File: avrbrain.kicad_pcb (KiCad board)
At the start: 2 copper layers, 85 x 56 mm, 61 parts, among them J1 UPDI, J11 UEXT, J12 SM04B-SRSS-TB, J2 PORTD, J3 PORTG, J4 PORTE, J5 PORTA, J6 PORTB, J7 PORTC, J8 XKTF-0803-0, J9 U254-051T-4BH81-S2S, Q1 BSS138, SW1 RESET, SW3 PROG_EN, U1 AVR128DB64x-xPT, U2 AMS1117-3.3, U3 CH340C, U4 PCF8563T, Y1 32kHz

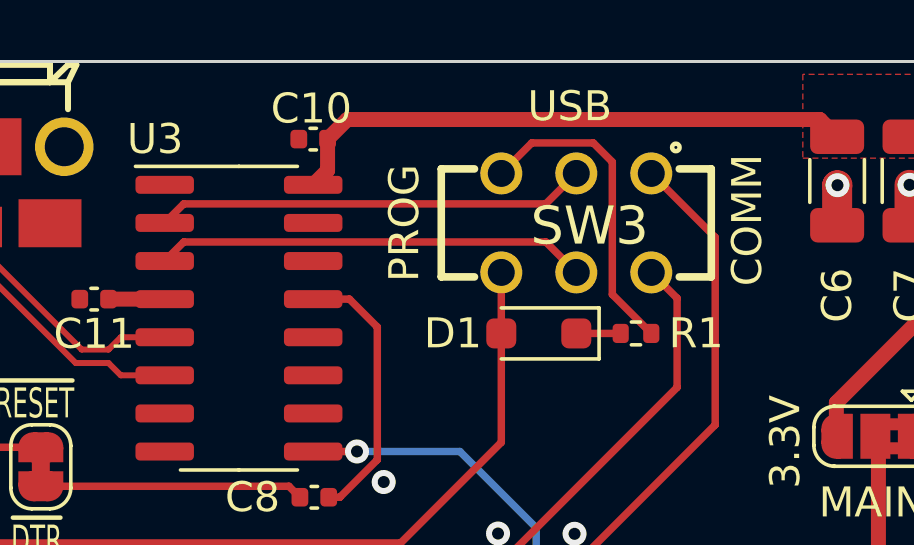
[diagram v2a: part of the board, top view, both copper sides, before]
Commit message: Put resistor before switch to avoid parasitic powering of the board
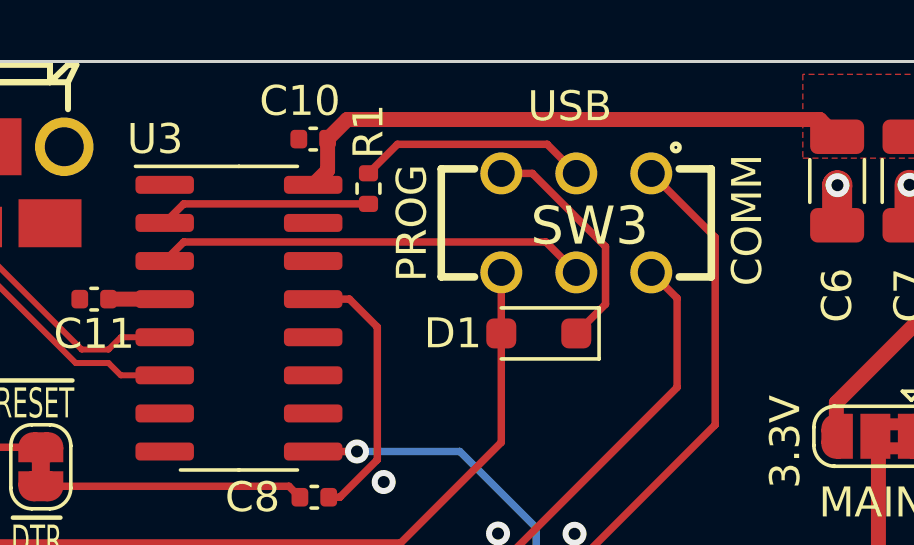
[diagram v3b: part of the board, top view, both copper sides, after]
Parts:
- R1: value 4.7K -> 1K
- moved R1 10.1 mm to (146.8, 85.2), turned to 90 degrees
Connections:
- R1 pad 1: Net-(SW3A-C) -> Net-(U3-TXD)
- R1 pad 2: Net-(D1-K) -> /Peripherals/USBTX
- SW3 pad 3: Net-(SW3A-C) -> Net-(D1-K)
- U3 pad 2: /Peripherals/USBTX -> Net-(U3-TXD)
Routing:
- net Net-(SW3A-C): track 10.6 -> 0.00 mm
- net Net-(U3-TXD): track 0.00 -> 7.06 mm
- net /Peripherals/USBTX: track 14.4 -> 7.73 mm
- net Net-(D1-K): track 1.48 -> 7.78 mm
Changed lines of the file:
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@@
   (net 79 "Net-(JP2-B)")
   (net 80 "Net-(JP3-B)")
-  (net 81 "Net-(SW3A-C)")
+  (net 81 "Net-(U3-TXD)")
   (net 82 "/Peripherals/USBTX")
   (net 83 "/Peripherals/USBRX")
@@
       (net 2 "GND") (pinfunction "GND") (pintype "power_in"))
     (pad "2" smd roundrect (at -2.475 -3.175) (size 1.95 0.6) (layers "F.Cu" "F.Paste" "F.Mask") (roundrect_rratio 0.25)
-      (net 82 "/Peripherals/USBTX") (pinfunction "TXD") (pintype "output"))
+      (net 81 "Net-(U3-TXD)") (pinfunction "TXD") (pintype "output"))
     (pad "3" smd roundrect (at -2.475 -1.905) (size 1.95 0.6) (layers "F.Cu" "F.Paste" "F.Mask") (roundrect_rratio 0.25)
       (net 83 "/Peripherals/USBRX") (pinfunction "RXD") (pintype "input"))
@@
       (net 82 "/Peripherals/USBTX") (pinfunction "B") (pintype "passive"))
     (pad "3" thru_hole circle (at 2.5 1.65 180) (size 1.4 1.4) (drill 0.9) (layers "*.Cu" "*.Mask")
-      (net 81 "Net-(SW3A-C)") (pinfunction "C") (pintype "passive"))
+      (net 49 "Net-(D1-K)") (pinfunction "C") (pintype "passive"))
     (pad "4" thru_hole circle (at -2.5 -1.65 180) (size 1.4 1.4) (drill 0.9) (layers "*.Cu" "*.Mask")
       (net 41 "TXF") (pinfunction "A") (pintype "passive"))
@@
     (fp_arc (start 4.02 5.42) (mid 4.121556 5.533647) (end 4.22 5.65)
       (stroke (width 0.05) (type solid)) (layer "F.CrtYd"))
-    (fp_arc (start 5.3 6.1) (mid 4.714387 5.984475) (end 4.22 5.65)
+    (fp_arc (start 5.3 6.1) (mid 4.714381 5.984481) (end 4.22 5.65)
       (stroke (width 0.05) (type solid)) (layer "F.CrtYd"))
     (fp_arc (start 7.25 -1.94) (mid 8.650198 0.005) (end 7.25 1.95)
       (stroke (width 0.05) (type solid)) (layer "F.CrtYd"))
-    (fp_arc (start 7.25 4.1) (mid 6.682004 5.496828) (end 5.3 6.1)
+    (fp_arc (start 7.25 4.1) (mid 6.682004 5.496829) (end 5.3 6.1)
       (stroke (width 0.05) (type solid)) (layer "F.CrtYd"))
     (fp_line (start -6.6 -3.4) (end -6.6 4.05)
@@
     (fp_arc (start 5.378013 5.447558) (mid 4.942442 5.378013) (end 4.6 5.1)
       (stroke (width 0.1) (type solid)) (layer "F.Fab"))
-    (fp_arc (start 6.6 4.1) (mid 6.222442 5.03735) (end 5.3 5.45)
+    (fp_arc (start 6.6 4.1) (mid 6.222443 5.037354) (end 5.3 5.45)
       (stroke (width 0.1) (type solid)) (layer "F.Fab"))
     (pad "1" thru_hole circle (at -6.6 0) (size 3 3) (drill 1.9) (layers "*.Cu" "*.Mask")
@@
   )
   (footprint "Resistor_SMD:R_0402_1005Metric" (layer "F.Cu")
-    (at 155.7285 90.043 180)
+    (at 146.812 85.215 90)
     (descr "Resistor SMD 0402 (1005 Metric), square (rectangular) end terminal, IPC_7351 nominal, (Body size source: IPC-SM-782 page 72, https://www.pcb-3d.com/wordpress/wp-content/uploads/ipc-sm-782a_amendment_1_and_2.pdf), generated with kicad-footprint-generator")
     (tags "resistor")
@@
     (property "ki_keywords" "R resistor")
     (attr smd)
-    (fp_text reference "R1" (at -2.0055 0) (layer "F.SilkS")
+    (fp_text reference "R1" (at 1.903 0 90) (layer "F.SilkS")
         (effects (font (size 1 1) (thickness 0.15)))
     )
-    (fp_text value "4.7K" (at 0 1.17) (layer "F.Fab")
+    (fp_text value "1K" (at 0 1.17 90) (layer "F.Fab")
         (effects (font (size 1 1) (thickness 0.15)))
     )
-    (fp_text user "${REFERENCE}" (at 0 0) (layer "F.Fab")
+    (fp_text user "${REFERENCE}" (at 0 0 90) (layer "F.Fab")
         (effects (font (size 0.26 0.26) (thickness 0.04)))
     )
@@
     (fp_line (start 0.525 0.27) (end -0.525 0.27)
       (stroke (width 0.1) (type solid)) (layer "F.Fab"))
-    (pad "1" smd roundrect (at -0.51 0 180) (size 0.54 0.64) (layers "F.Cu" "F.Paste" "F.Mask") (roundrect_rratio 0.25)
-      (net 81 "Net-(SW3A-C)") (pintype "passive"))
-    (pad "2" smd roundrect (at 0.51 0 180) (size 0.54 0.64) (layers "F.Cu" "F.Paste" "F.Mask") (roundrect_rratio 0.25)
-      (net 49 "Net-(D1-K)") (pintype "passive"))
+    (pad "1" smd roundrect (at -0.51 0 90) (size 0.54 0.64) (layers "F.Cu" "F.Paste" "F.Mask") (roundrect_rratio 0.25)
+      (net 81 "Net-(U3-TXD)") (pintype "passive"))
+    (pad "2" smd roundrect (at 0.51 0 90) (size 0.54 0.64) (layers "F.Cu" "F.Paste" "F.Mask") (roundrect_rratio 0.25)
+      (net 82 "/Peripherals/USBTX") (pintype "passive"))
     (model "${KICAD6_3DMODEL_DIR}/Resistor_SMD.3dshapes/R_0402_1005Metric.wrl"
       (offset (xyz 0 0 0))
@@
     (property "ki_keywords" "capacitor cap")
     (attr smd)
-    (fp_text reference "C10" (at 0.062 1.016) (layer "F.SilkS")
+    (fp_text reference "C10" (at 0.443 1.27) (layer "F.SilkS")
         (effects (font (size 1 1) (thickness 0.15)))
     )
@@
     (effects (font (size 1 1) (thickness 0.15)) (justify left bottom))
   )
-  (gr_text "PROG" (at 148.59 88.325025 90) (layer "F.SilkS")
+  (gr_text "PROG" (at 148.844 88.325025 90) (layer "F.SilkS")
     (effects (font (size 1 1) (thickness 0.15)) (justify left bottom))
   )
@@
   (segment (start 195.052 121.92) (end 195.814 122.682) (width 0.5) (layer "F.Cu") (net 48))
   (segment (start 205.585 125.758) (end 205.105 126.238) (width 0.5) (layer "F.Cu") (net 48))
-  (segment (start 153.7385 90.043) (end 155.2185 90.043) (width 0.25) (layer "F.Cu") (net 49))
+  (segment (start 152.273 84.709) (end 151.2385 84.709) (width 0.25) (layer "F.Cu") (net 49))
+  (segment (start 154.7135 89.068) (end 154.7135 87.1495) (width 0.25) (layer "F.Cu") (net 49))
+  (segment (start 154.7135 87.1495) (end 152.273 84.709) (width 0.25) (layer "F.Cu") (net 49))
+  (segment (start 153.7385 90.043) (end 154.7135 89.068) (width 0.25) (layer "F.Cu") (net 49))
   (segment (start 124.46 99.06) (end 125.033485 99.06) (width 0.25) (layer "F.Cu") (net 50))
   (segment (start 147.885686 97.028) (end 151.2385 93.675186) (width 0.25) (layer "F.Cu") (net 50))
@@
   (segment (start 186.436 120.368971) (end 186.436 122.936) (width 0.25) (layer "F.Cu") (net 80))
   (segment (start 190.754 127.254) (end 190.754 131.318) (width 0.25) (layer "F.Cu") (net 80))
-  (segment (start 154.305 83.693) (end 152.2545 83.693) (width 0.25) (layer "F.Cu") (net 81))
-  (segment (start 156.2385 90.043) (end 154.94 88.7445) (width 0.25) (layer "F.Cu") (net 81))
-  (segment (start 154.94 88.7445) (end 154.94 84.328) (width 0.25) (layer "F.Cu") (net 81))
-  (segment (start 154.94 84.328) (end 154.305 83.693) (width 0.25) (layer "F.Cu") (net 81))
-  (segment (start 152.2545 83.693) (end 151.2385 84.709) (width 0.25) (layer "F.Cu") (net 81))
-  (segment (start 140.654 85.725) (end 152.7225 85.725) (width 0.25) (layer "F.Cu") (net 82))
-  (segment (start 140.019 86.36) (end 140.654 85.725) (width 0.25) (layer "F.Cu") (net 82))
-  (segment (start 152.7225 85.725) (end 153.7385 84.709) (width 0.25) (layer "F.Cu") (net 82))
+  (segment (start 140.654 85.725) (end 146.812 85.725) (width 0.25) (layer "F.Cu") (net 81))
+  (segment (start 140.019 86.36) (end 140.654 85.725) (width 0.25) (layer "F.Cu") (net 81))
+  (segment (start 152.768604 83.739104) (end 153.7385 84.709) (width 0.25) (layer "F.Cu") (net 82))
+  (segment (start 146.812 84.705) (end 147.777896 83.739104) (width 0.25) (layer "F.Cu") (net 82))
+  (segment (start 147.777896 83.739104) (end 152.768604 83.739104) (width 0.25) (layer "F.Cu") (net 82))
   (segment (start 140.654 86.995) (end 152.7245 86.995) (width 0.25) (layer "F.Cu") (net 83))
   (segment (start 152.7245 86.995) (end 153.7385 88.009) (width 0.25) (layer "F.Cu") (net 83))

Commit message: Final touches
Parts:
- added C16: 1uf, Capacitor_SMD:C_1206_3216Metric, F.Cu at (141.0, 117.0)
- added C17: 1uf, Capacitor_SMD:C_1206_3216Metric, F.Cu at (163.6, 118.9)
- added J10: PORTF, Connector_PinSocket_2.54mm:PinSocket_1x02_P2.54mm_Vertical, F.Cu at (165.1, 109.2)
- moved C4 0.51 mm to (144.7, 116.8)
- moved C3 0.33 mm to (155.4, 109.3)
- moved C2 0.13 mm to (151.4, 124.2)
- moved C5 0.13 mm to (159.9, 118.8)
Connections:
- U1 pad 48: RXF -> TXF
- U1 pad 49: TXF -> RXF
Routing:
- net VDD: track 148.2 -> 155.2 mm
- net GND: track 19.5 -> 22.7 mm
- net TXF: track 30.1 -> 28.1 mm
- net VDDF: track 52.5 -> 53.8 mm
- net RXF: track 33.4 -> 34.6 mm
- net ~{CTS}: track 24.4 -> 23.6 mm
- net Net-(JP7-B): track 15.1 -> 15.8 mm
- net /PG3: track 15.2 -> 15.8 mm
- net TXC: track 77.3 -> 77.9 mm
- net SCL: track 87.6 -> 88.1 mm
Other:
- board text added: "3V3"
- board text added: "F0"
- board text added: "F1"
- board text added: "GND"
- board text added: "MISO"
- board text added: "MOSI"
- board text added: "RX"
- board text added: "SCK"
- board text added: "TX"
- board text added: "~{CS}"

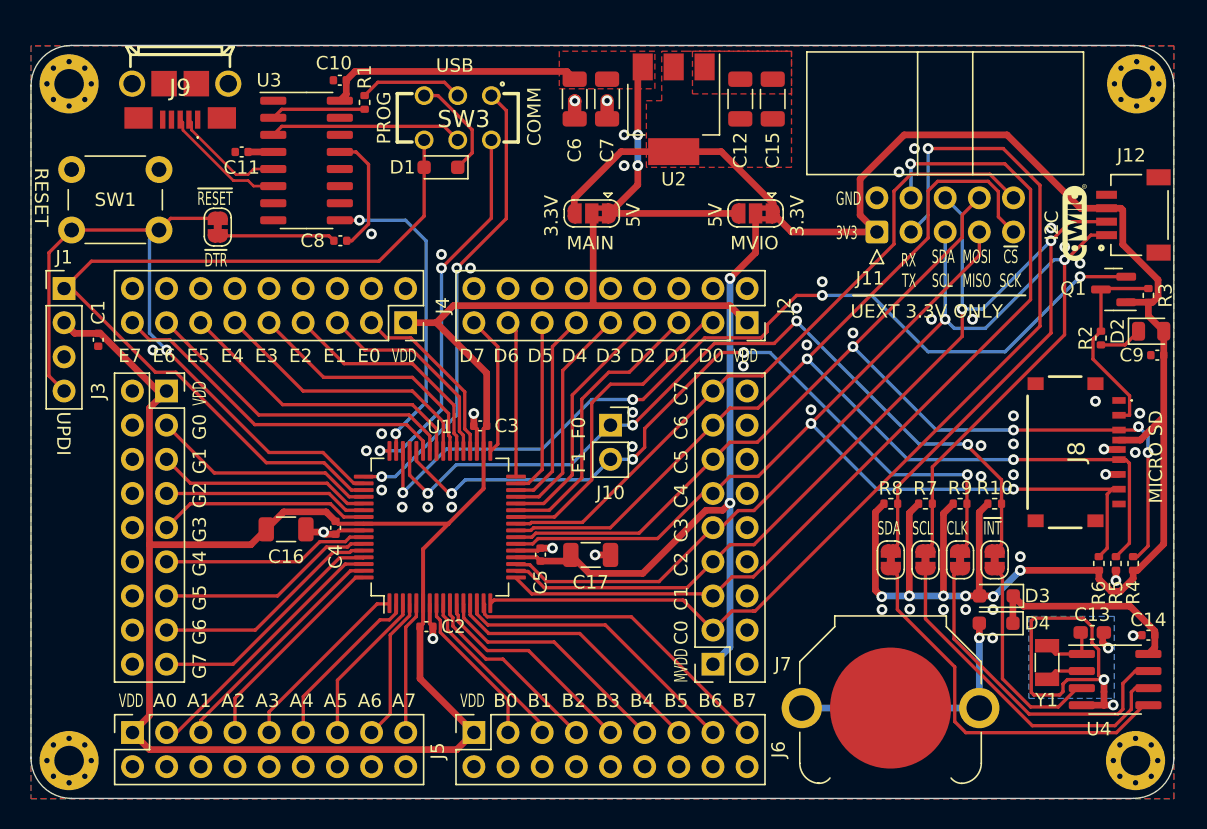
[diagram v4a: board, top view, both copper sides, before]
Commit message: Switch to 4 layer; reduce connector size and move to edge
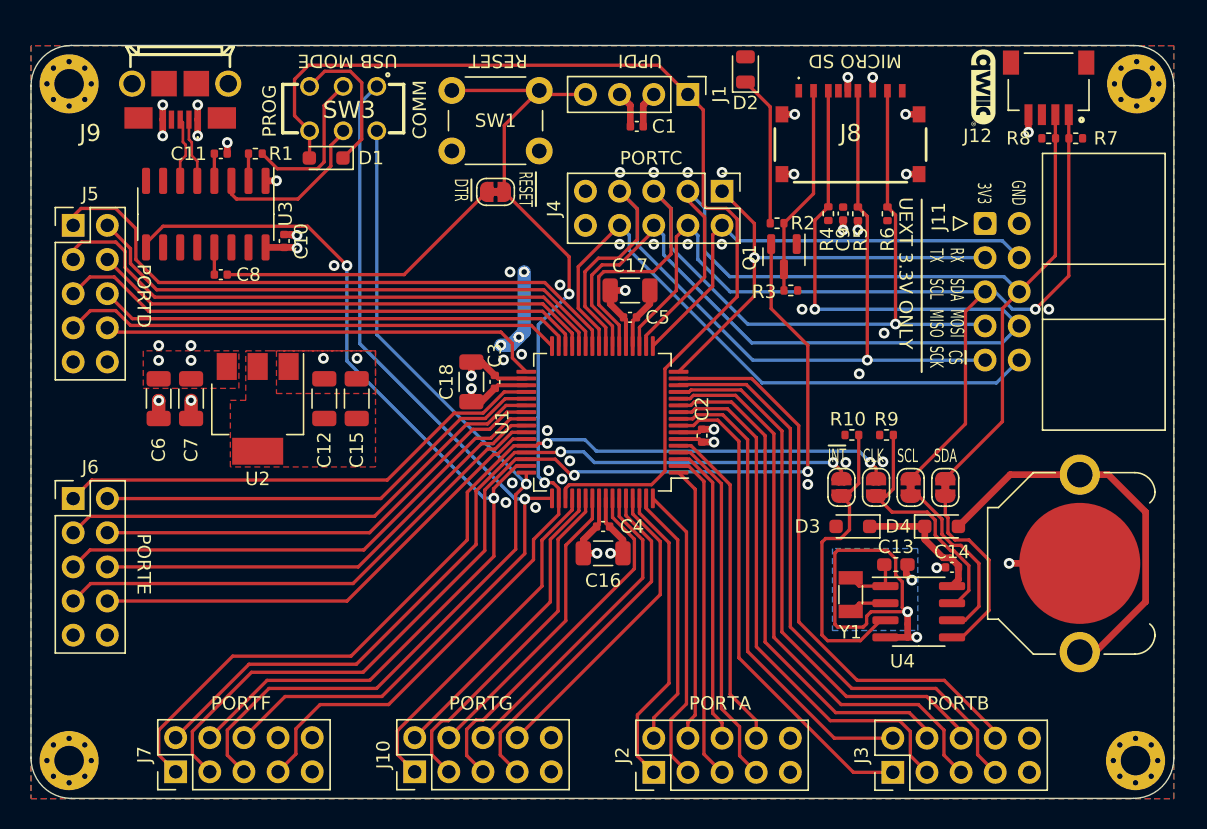
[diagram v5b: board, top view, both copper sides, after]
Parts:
- removed JP4: VDD_MAIN, Jumper:SolderJumper-3_P1.3mm_Bridged2Bar12_RoundedPad1.0x1.5mm
- removed JP5: VDD_MVIO, Jumper:SolderJumper-3_P1.3mm_Bridged2Bar12_RoundedPad1.0x1.5mm
- added C18: 1uf, Capacitor_SMD:C_1206_3216Metric, F.Cu at (154.8, 106.0)
- J10: value PORTF -> PORTG; footprint Connector_PinSocket_2.54mm:PinSocket_1x02_P2.54mm_Vertical -> Connector_PinHeader_2.54mm:PinHeader_2x05_P2.54mm_Vertical
- J2: value PORTD -> PORTA; footprint Connector_PinSocket_2.54mm:PinSocket_2x09_P2.54mm_Vertical -> Connector_PinHeader_2.54mm:PinHeader_2x05_P2.54mm_Vertical
- J3: value PORTG -> PORTB; footprint Connector_PinSocket_2.54mm:PinSocket_2x09_P2.54mm_Vertical -> Connector_PinHeader_2.54mm:PinHeader_2x05_P2.54mm_Vertical
- J4: value PORTE -> PORTC; footprint Connector_PinSocket_2.54mm:PinSocket_2x09_P2.54mm_Vertical -> Connector_PinHeader_2.54mm:PinHeader_2x05_P2.54mm_Vertical
- J5: value PORTA -> PORTD; footprint Connector_PinSocket_2.54mm:PinSocket_2x09_P2.54mm_Vertical -> Connector_PinHeader_2.54mm:PinHeader_2x05_P2.54mm_Vertical
- J6: value PORTB -> PORTE; footprint Connector_PinSocket_2.54mm:PinSocket_2x09_P2.54mm_Vertical -> Connector_PinHeader_2.54mm:PinHeader_2x05_P2.54mm_Vertical
- J7: value PORTC -> PORTF; footprint Connector_PinSocket_2.54mm:PinSocket_2x09_P2.54mm_Vertical -> Connector_PinHeader_2.54mm:PinHeader_2x05_P2.54mm_Vertical
- JP6, JP7: footprint Jumper:SolderJumper-2_P1.3mm_Bridged_RoundedPad1.0x1.5mm -> Jumper:SolderJumper-2_P1.3mm_Open_RoundedPad1.0x1.5mm
- moved J3 61.0 mm to (186.1, 135.0), turned to 90 degrees
- moved J1 48.6 mm to (170.9, 84.6), turned to -90 degrees
- moved C1 43.1 mm to (167.1, 87.0), turned to 180 degrees
- moved J7 40.8 mm to (132.8, 135.0), turned to 90 degrees
- moved C12 38.1 mm to (143.8, 107.2)
- moved C15 38.1 mm to (146.2, 107.2)
- moved C6 38.1 mm to (131.5, 107.2)
- moved C7 38.1 mm to (133.9, 107.2)
- moved U2 38.1 mm to (138.9, 108.0)
- moved J5 38.0 mm to (125.1, 94.4), turned to 0 degrees
- moved D2 35.9 mm to (175.1, 82.8), turned to 90 degrees
- moved SW1 34.8 mm to (159.8, 88.8), turned to 180 degrees
- moved J6 34.5 mm to (125.1, 114.7), turned to 0 degrees
- moved R4 34.5 mm to (181.3, 93.5)
- moved J2 34.2 mm to (168.3, 135.0), turned to 90 degrees
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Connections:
- C1 pad 1: VDD -> +5V
- C16 pad 2: VDD -> +5V
- C17 pad 1: VDDF -> GND
- C17 pad 2: GND -> +3.3V
- C2 pad 2: VDD -> +5V
- C3 pad 2: VDD -> +5V
- C4 pad 1: VDD -> +5V
- C5 pad 1: VDDF -> +3.3V
- J1 pad 2: VDD -> +5V
- J10 pad 1: ~{RTCINT} -> /PG0
- J10 pad 2: CLK32K -> /PG1
- J2 pad 1: VDD -> /PA0
- J2 pad 10: GND -> +5V
- J2 pad 2: GND -> /PA1
- J2 pad 3: /PD0 -> /PA2
- J2 pad 4: GND -> /PA3
- J2 pad 5: /PD1 -> /PA4
- J2 pad 6: GND -> /PA5
- J2 pad 7: /PD2 -> /PA6
- J2 pad 8: GND -> /PA7
- J2 pad 9: /PD3 -> GND
- J3 pad 1: VDD -> /PB0
- J3 pad 10: GND -> +5V
- J3 pad 2: GND -> /PB1
- J3 pad 3: /PG0 -> /PB2
- J3 pad 4: GND -> /PB3
- J3 pad 5: /PG1 -> /PB4
- J3 pad 6: GND -> /PB5
- J3 pad 7: /PG2 -> /PB6
- J3 pad 8: GND -> /PB7
- J3 pad 9: /PG3 -> GND
- J4 pad 1: VDD -> TXC
- J4 pad 10: GND -> +3.3V
- J4 pad 2: GND -> RXC
- J4 pad 3: /PE0 -> SDA
- J4 pad 4: GND -> SCL
- J4 pad 5: /PE1 -> MISO
- J4 pad 6: GND -> MOSI
- J4 pad 7: /PE2 -> SCK
- J4 pad 8: GND -> ~{CS}
- J4 pad 9: /PE3 -> GND
- J5 pad 1: VDD -> /PD0
- J5 pad 10: GND -> +5V
- J5 pad 2: GND -> /PD1
- J5 pad 3: /PA0 -> /PD2
- J5 pad 4: GND -> /PD3
- J5 pad 5: /PA1 -> /PD4
- J5 pad 6: GND -> /PD5
- J5 pad 7: /PA2 -> /PD6
- J5 pad 8: GND -> /PD7
- J5 pad 9: /PA3 -> GND
- J6 pad 1: VDD -> /PE0
- J6 pad 10: GND -> +5V
- J6 pad 2: GND -> /PE1
- J6 pad 3: /PB0 -> /PE2
- J6 pad 4: GND -> /PE3
- J6 pad 5: /PB1 -> /PE4
- J6 pad 6: GND -> /PE5
- J6 pad 7: /PB2 -> /PE6
- J6 pad 8: GND -> /PE7
- J6 pad 9: /PB3 -> GND
- J7 pad 1: VDDF -> CLK32K
- J7 pad 10: GND -> +5V
- J7 pad 2: GND -> ~{RTCINT}
- J7 pad 3: TXC -> ~{SDCS}
- J7 pad 4: GND -> ~{CTS}
- J7 pad 5: RXC -> TXF
- J7 pad 6: GND -> RXF
- J7 pad 7: SDA -> ~{RESET}
- J7 pad 8: GND -> unconnected-(J7-Pin_8-Pad8)
- J7 pad 9: SCL -> GND
- J9 pad 1: unconnected-(J9-VBUS-Pad1) -> +5V
- R10 pad 2: ~{RTCINT} -> Net-(JP7-B)
- R9 pad 2: CLK32K -> Net-(JP6-B)
- U1 pad 20: VDDF -> +3.3V
- U1 pad 34: VDD -> +5V
- U1 pad 56: VDD -> +5V
- U1 pad 6: VDD -> +5V
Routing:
- net VDD: track 155.2 -> 0.00 mm
- net +3.3V: track 141.8 -> 11.3 mm, vias 6 -> 3
- net VDDF: track 53.8 -> 0.00 mm, vias 2 -> 0
- net ~{CTS}: track 23.6 -> 74.1 mm
- net TXC: track 77.9 -> 33.9 mm
- net TXF: track 28.1 -> 67.5 mm, vias 2 -> 1
- net RXF: track 34.6 -> 69.4 mm, vias 2 -> 1
- net RXC: track 68.4 -> 34.2 mm, vias 1 -> 0
- net /PB2: track 14.2 -> 39.9 mm
- net /PD6: track 11.7 -> 37.2 mm
- net /PD4: track 15.0 -> 39.8 mm
- net /PD2: track 18.6 -> 43.3 mm
- net /PB4: track 18.0 -> 42.7 mm
- net /PB0: track 11.8 -> 36.4 mm
- net ~{RESET}: track 52.9 -> 77.4 mm, vias 1 -> 2
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- added copper zone on B.Cu, net +5V
- added copper zone on In1.Cu, net GND
- added copper zone on In2.Cu, net GND
- removed copper zone on B.Cu, net GND
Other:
- copper layers 2 -> 4
- board text added: "Copyright (C)2024 J.B. Langston https://github.com/jblang/avrbrain"
- board text added: "PORTA"
- board text added: "PORTB"
- board text added: "PORTC"
- board text added: "PORTD"
- board text added: "PORTE"
- board text added: "PORTF"
- board text added: "PORTG"
- board text added: "USB MODE"
- board text removed: "3.3V"
- board text removed: "5V"
- board text removed: "A0"
- board text removed: "A1"
- board text removed: "A2"
- board text removed: "A3"
- board text removed: "A4"
- board text removed: "A5"
- board text removed: "A6"
- board text removed: "A7"
- board text removed: "B0"
- board text removed: "B1"
- board text removed: "B2"
- board text removed: "B3"
- board text removed: "B4"
- board text removed: "B5"
- board text removed: "B6"
- board text removed: "B7"
- board text removed: "C0"
- board text removed: "C1"
- board text removed: "C2"
- board text removed: "C3"
- board text removed: "C4"
- board text removed: "C5"
- board text removed: "C6"
- board text removed: "C7"
- board text removed: "Copyright (C)2024 J.B. Langston III https://github.com/jblang/avrbrain"
- board text removed: "D0"
- board text removed: "D1"
- board text removed: "D2"
- board text removed: "D3"
- board text removed: "D4"
- board text removed: "D5"
- board text removed: "D6"
- board text removed: "D7"
- board text removed: "E0"
- board text removed: "E1"
- board text removed: "E2"
- board text removed: "E3"
- board text removed: "E4"
- board text removed: "E5"
- board text removed: "E6"
- board text removed: "E7"
- board text removed: "F0"
- board text removed: "F1"
- board text removed: "G0"
- board text removed: "G1"
- board text removed: "G2"
- board text removed: "G3"
- board text removed: "G4"
- board text removed: "G5"
- board text removed: "G6"
- board text removed: "G7"
- board text removed: "I2C"
- board text removed: "MAIN"
- board text removed: "MVDD"
- board text removed: "MVIO"
- board text removed: "USB"
- board text removed: "VDD"
